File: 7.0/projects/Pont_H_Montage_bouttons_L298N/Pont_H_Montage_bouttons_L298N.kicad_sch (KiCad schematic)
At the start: 28 parts, among them M1 Motor_DC, U1 L298N, U2 L7805

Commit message: TP1
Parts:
- removed ANTI-HORAIRE: SW_A2, symbol Switch:SW_Push
- removed POWER_SUPPLY: VS(3) GND(2) LOGIC(1), symbol Connector:Conn_01x03_Pin
- added ANTIHORAIRE2: SW_A2, symbol Switch:SW_Push
- added POWER_SUPPLY1: VS(3) GND(2) LOGIC(1), symbol Connector:Screw_Terminal_01x03
- renumbered HORAIRE to HORAIRE1, OUT_MA to OUT_MA1, OUT_MB to OUT_MB2, V_EXTERNE to V_EXTERNE1
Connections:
- net GND: now also POWER_SUPPLY1.2 (Pin_2)
- net IN2: now also ANTIHORAIRE2.1
- net VS: now also POWER_SUPPLY1.3 (Pin_3)
- net VSS_5V: now also ANTIHORAIRE2.2, POWER_SUPPLY1.1 (Pin_1)

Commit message: adding all circuits
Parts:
- added V_EXTERNE2: 5VDC, symbol Simulation_SPICE:VDC
- JP1: symbol Jumper:Jumper_2_Bridged -> Jumper:Jumper_2_Open
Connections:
- net GND: now also V_EXTERNE2.2; no longer POWER_SUPPLY1.2 (Pin_2)
- net VSS_5V renamed VSS
- net VSS: now also V_EXTERNE2.1
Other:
- moved on the sheet: ANTIHORAIRE2, C1, C2, CONTROL_INPUTS_1, CONTROL_INPUTS_2, D1, D2, D3, D4, D5, D6, D7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

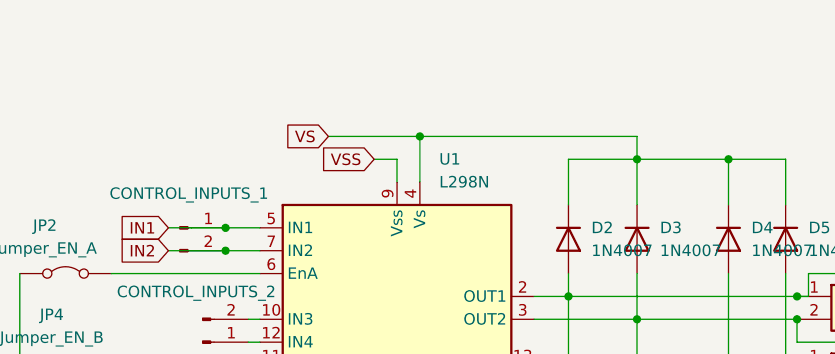
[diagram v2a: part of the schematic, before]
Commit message: adding 7 segment display
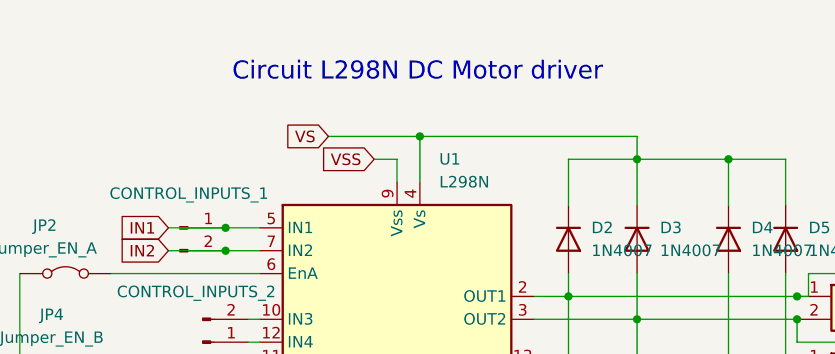
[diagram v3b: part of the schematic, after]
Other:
- note added: "Circuit L298N DC Motor driver"
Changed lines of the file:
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@@
+		)
+	)
+	(text "Circuit L298N DC Motor driver"
+		(exclude_from_sim no)
+		(at 126.746 74.168 0)
+		(effects
+			(font
+				(size 2 2)
+			)
 		)
 	)
